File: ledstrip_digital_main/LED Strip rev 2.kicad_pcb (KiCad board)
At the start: 2 copper layers, 28 parts, among them P1 STRIP, P2 SWD, SW1 SW_PUSH, U1 STM32F051K8U8, U2 TSC888B, X1 8M

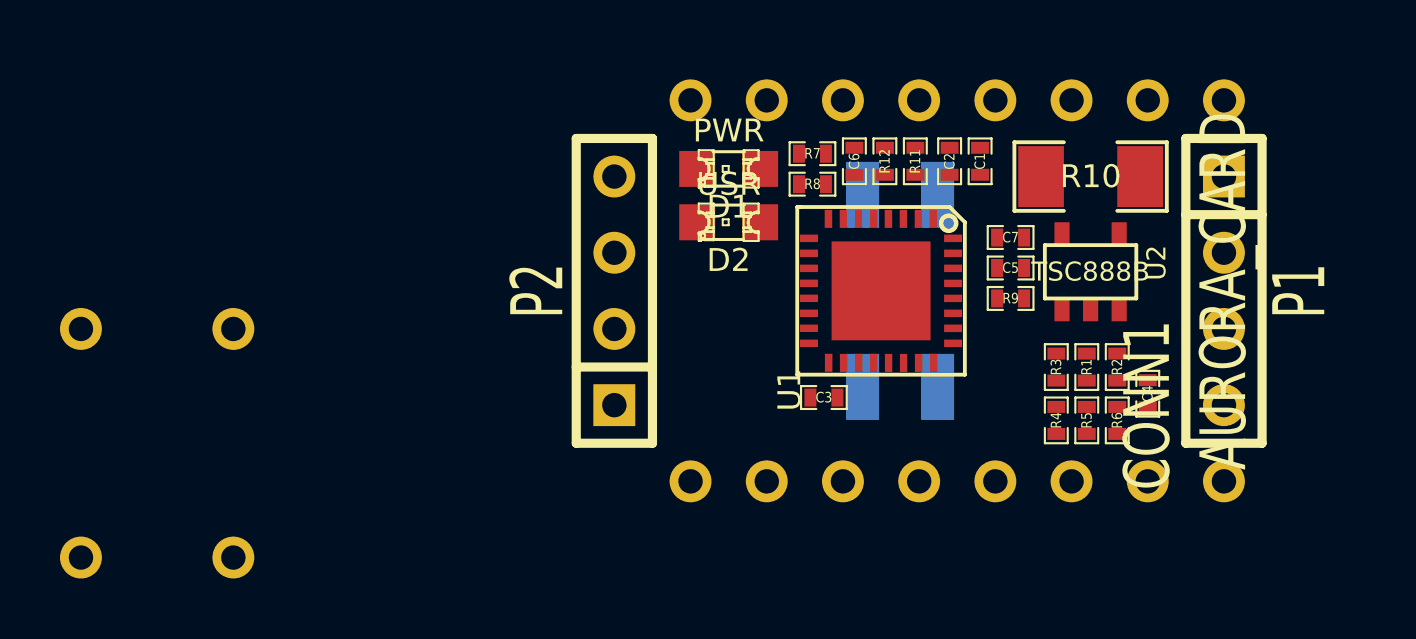
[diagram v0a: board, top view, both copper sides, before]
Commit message: finished copper for motherboard
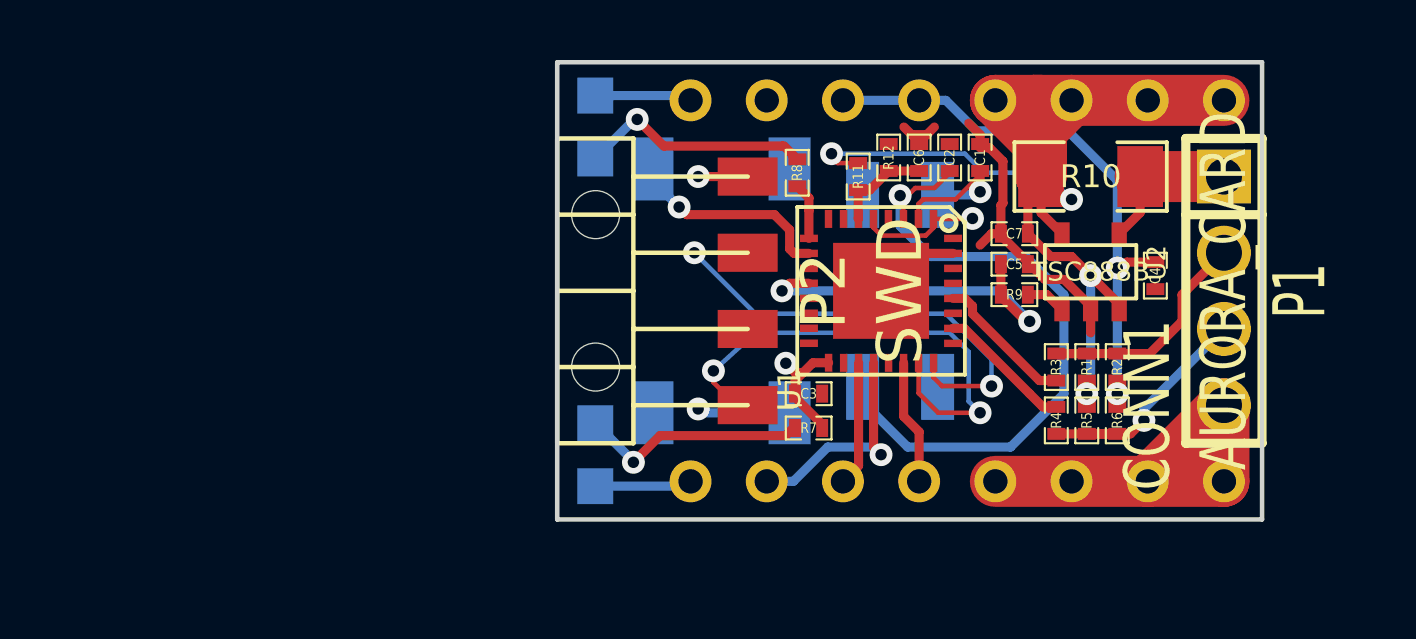
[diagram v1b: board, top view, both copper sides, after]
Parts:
- D1, D2: moved to B.Cu
- P2: footprint SIL-4 -> SMD-HDR-4
- SW1: value SW_PUSH -> TACT; footprint SW_PUSH_SMALL -> TACT-SW-SMD
- moved SW1 19.5 mm to (218.2, 148.6), turned to 0 degrees
- moved D1 10.5 mm to (214.0, 154.1), turned to 270 degrees
- moved R7 9.14 mm to (221.1, 153.2)
- moved D2 5.46 mm to (214.0, 143.1), turned to 90 degrees
- moved P2 4.44 mm to (219.1, 148.6), turned to 270 degrees
- moved C4 3.95 mm to (232.7, 148.1)
- moved C6 2.16 mm to (224.8, 144.1)
- moved R11 1.97 mm to (222.8, 144.8)
- moved R8 0.64 mm to (220.7, 144.7), turned to 270 degrees
- moved C3 0.52 mm to (221.1, 152.0)
- moved C5 0.18 mm to (228.0, 147.7)
- moved C7 0.18 mm to (228.0, 146.7)
- moved R12 0.18 mm to (223.8, 144.1)
- moved R9 0.18 mm to (228.0, 148.7)
- moved C1 0.13 mm to (226.8, 144.1)
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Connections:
- CONN1 pad 5: GND -> /HP_GND
- CONN1 pad 6: GND -> /HP_GND
- CONN1 pad 7: GND -> /HP_GND
- CONN1 pad 8: GND -> /HP_GND
- P1 pad 4: GND -> /HP_GND
- SW1 pad 2: /USR_BTN -> (no net)
- U1 pad 12: (no net) -> /I_LED
- U1 pad 7: /I_LED -> (no net)
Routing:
- net +12V: track 0.00 -> 45.1 mm, vias 0 -> 4
- net GND: track 0.00 -> 24.4 mm, vias 0 -> 1
- net /OSC_OUT: track 0.00 -> 21.8 mm, vias 0 -> 1
- net +5V: track 0.00 -> 19.6 mm, vias 0 -> 2
- net /SWDAT: track 0.00 -> 17.0 mm, vias 0 -> 2
- net /SWCLK: track 0.00 -> 16.6 mm, vias 0 -> 2
- net /HP_GND: track 0.00 -> 16.3 mm
- net /I_LED: track 0.00 -> 12.1 mm, vias 0 -> 2
- net +3.3V: track 0.00 -> 9.78 mm, vias 0 -> 3
- net /LED_DAT: track 0.00 -> 8.59 mm
- net /LED_CLK: track 0.00 -> 8.28 mm, vias 0 -> 1
- net N-0000036: track 0.00 -> 7.82 mm, vias 0 -> 1
- net N-0000035: track 0.00 -> 7.72 mm, vias 0 -> 1
- net /RX: track 0.00 -> 7.55 mm, vias 0 -> 1
- net /USR_BTN: track 0.00 -> 6.98 mm, vias 0 -> 1
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- added copper zone on B.Cu, net +3.3V
- added copper zone on F.Cu, net GND
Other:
- board outline added: 23.5 x 15.2 mm
- net class Default: clearance 0.254 -> 0.1524; trace_width 0.254 -> 0.1524; via_dia 0.889 -> 0.762; via_drill 0.635 -> 0.381
- rule trace_clearance: 0.254 -> 0.1524
- rule trace_min: 0.254 -> 0.1524
- rule via_min_drill: 0.508 -> 0.381
- rule via_min_size: 0.889 -> 0.762

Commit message: fixed up silkscreen + made gerbers
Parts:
- D1, D2: footprint LED-0805 -> LED-0603
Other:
- board text added: "1"
- board text added: "CLK"
- board text added: "DAT"
- board text added: "GND"
- board text added: "PWR"

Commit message: Finished silkscreen on daughter board, it and digital led board are done\!
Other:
- board text added: "Aurora Project Digital LED Strip"
- board text added: "rev 1"
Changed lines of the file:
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@@
     (area 200.280002 135.326001 244.734733 158.247733)
     (thickness 1.6)
-    (drawings 11)
+    (drawings 13)
     (tracks 241)
     (zones 0)
@@
   (page A3)
   (layers
-    (15 F.Cu signal)
-    (0 B.Cu signal)
+    (15 F.Cu signal hide)
+    (0 B.Cu signal hide)
     (16 B.Adhes user)
     (17 F.Adhes user)
@@
   )
   (setup
-    (last_trace_width 0.3048)
+    (last_trace_width 0.1524)
     (user_trace_width 0.3048)
     (user_trace_width 1.7)
@@
     (pad_to_mask_clearance 0.2)
     (aux_axis_origin 0 0)
-    (visible_elements FFFFFFBF)
+    (visible_elements FFFFDFBF)
     (pcbplotparams
       (layerselection 284196865)
@@
   (module CX5 (layer B.Cu)
     (at 224.155 148.59 270)
-    (fp_text reference X1 (at -1.143 -3.302 270) (layer B.SilkS)
+    (fp_text reference X1 (at -4.826 0.127 360) (layer B.SilkS)
       (effects (font (size 0.762 0.762) (thickness 0.13)) (justify mirror))
     )
-    (fp_text value 8M (at 1.016 -3.302 270) (layer B.SilkS)
+    (fp_text value 8M (at 0 -0.127 270) (layer B.SilkS)
       (effects (font (size 0.762 0.762) (thickness 0.13)) (justify mirror))
     )
@@
     )
   )
-  (gr_text CLK (at 231.648 149.987) (layer B.SilkS)
-    (effects (font (size 1.5 1.5) (thickness 0.3)) (justify mirror))
-  )
-  (gr_text DAT (at 231.902 147.447) (layer B.SilkS)
-    (effects (font (size 1.5 1.5) (thickness 0.3)) (justify mirror))
-  )
-  (gr_text GND (at 231.521 152.527) (layer B.SilkS)
-    (effects (font (size 1.5 1.5) (thickness 0.3)) (justify mirror))
-  )
-  (gr_text PWR (at 231.521 144.907) (layer B.SilkS)
-    (effects (font (size 1.5 1.5) (thickness 0.3)) (justify mirror))
+  (gr_text "rev 1" (at 229.743 149.987 90) (layer B.SilkS)
+    (effects (font (size 0.762 0.762) (thickness 0.13)) (justify mirror))
+  )
+  (gr_text "Aurora Project\nDigital LED Strip\n" (at 227.457 148.59 90) (layer B.SilkS)
+    (effects (font (size 0.762 0.762) (thickness 0.13)) (justify mirror))
+  )
+  (gr_text CLK (at 232.283 149.987) (layer B.SilkS)
+    (effects (font (size 1 1) (thickness 0.2)) (justify mirror))
+  )
+  (gr_text DAT (at 232.537 147.447) (layer B.SilkS)
+    (effects (font (size 1 1) (thickness 0.2)) (justify mirror))
+  )
+  (gr_text GND (at 232.156 152.527) (layer B.SilkS)
+    (effects (font (size 1 1) (thickness 0.2)) (justify mirror))
+  )
+  (gr_text PWR (at 232.156 144.907) (layer B.SilkS)
+    (effects (font (size 1 1) (thickness 0.2)) (justify mirror))
   )
   (gr_text 1 (at 213.995 142.494) (layer F.SilkS)
